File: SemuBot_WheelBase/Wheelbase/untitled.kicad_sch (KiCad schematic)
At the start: 1 part, among them U1 STM32U575CITxQ

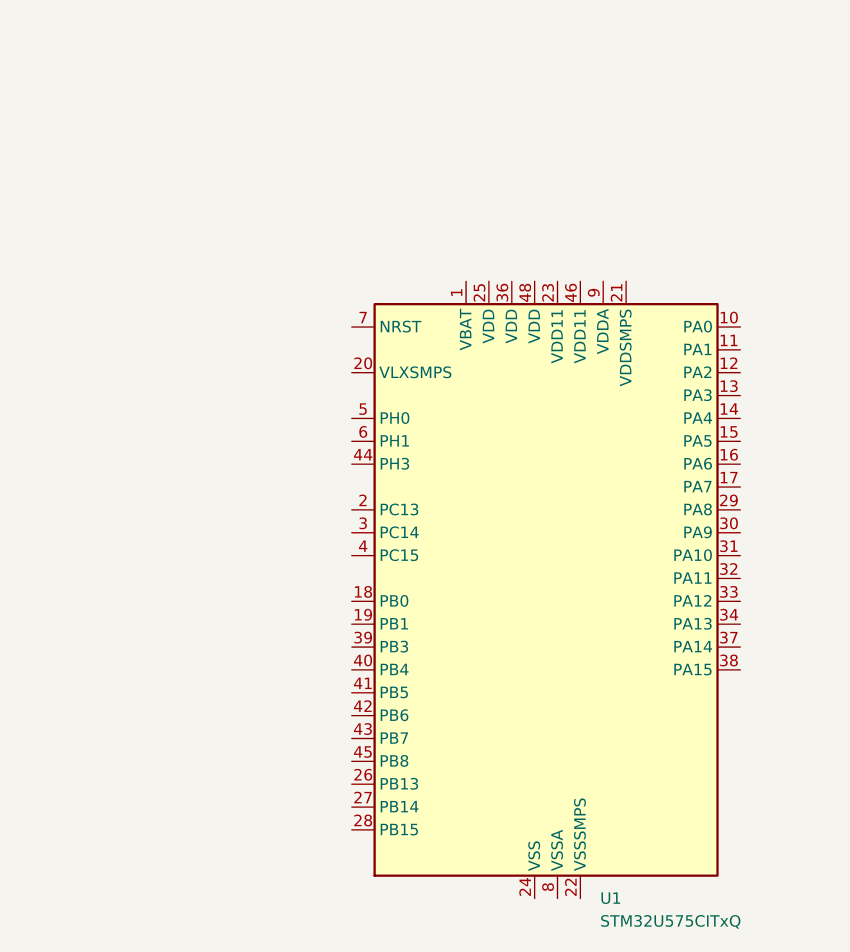
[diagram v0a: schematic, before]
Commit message: Wheelbase development and repo cleanup
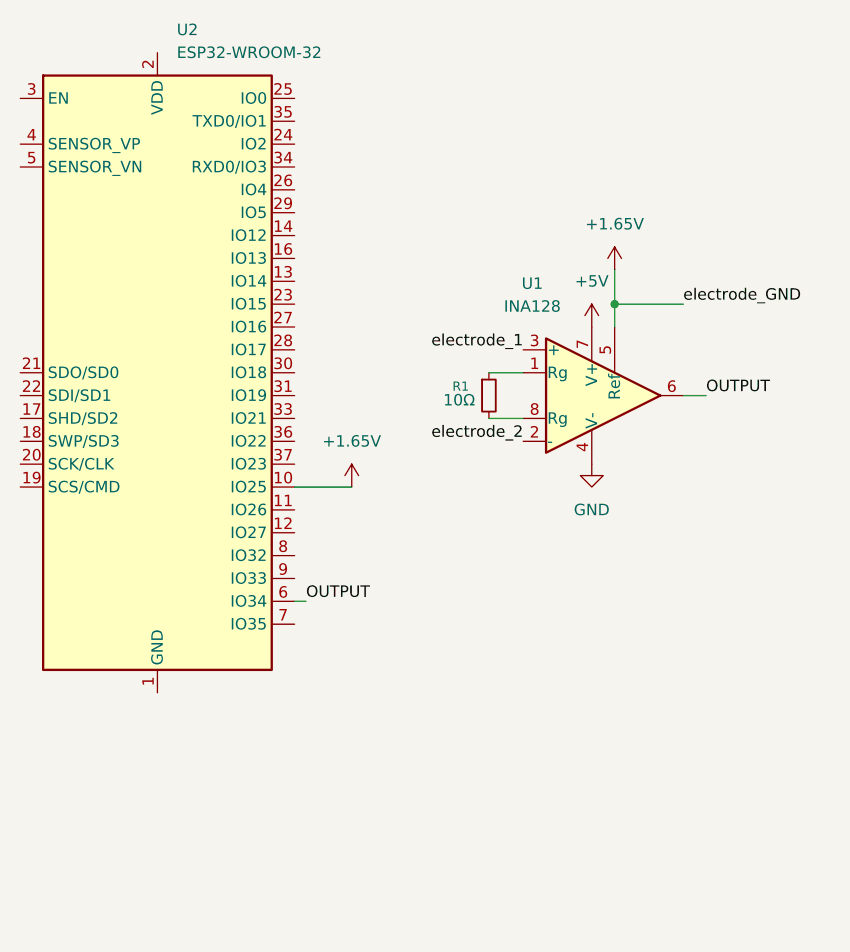
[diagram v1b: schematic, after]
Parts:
- removed U1: STM32U575CITxQ, Package_QFP:LQFP-48_7x7mm_P0.5mm, symbol MCU_ST_STM32U5:STM32U575CITxQ
- added R1: 10Ω, symbol Device:R_Small
- added U1: INA128, symbol Amplifier_Instrumentation:INA128
- added U2: ESP32-WROOM-32, RF_Module:ESP32-WROOM-32, symbol RF_Module:ESP32-WROOM-32
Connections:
- new net: R1.1, U1.1 (Rg)
- new net: R1.2, U1.8 (Rg)
- new net: U2.1 (GND), U2.15 (GND), U2.38 (GND), U2.39 (GND)
- new net +1.65V: U1.5 (Ref), U2.10 (IO25)
- new net +5V: U1.7 (V+)
- new net GND: U1.4 (V-)
- new net OUTPUT: U1.6, U2.6 (IO34)
- new net electrode_1: U1.3 (+)
- new net electrode_2: U1.2 (-)
